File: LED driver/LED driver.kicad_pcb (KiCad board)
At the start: 2 copper layers, 49 parts, among them J1 Conn_VCC, J2 Conn_LED, J3 Conn_UART, J4 Conn_01x10, P1 USB_C_Plug_USB2.0, Q1 IRFZ44NS, Q2 IRFZ44NS, Q3 IRFZ44NS, Q4 IRFZ44NS, Q5 IRFZ44NS, SW1 SW_Push, U1 ESP32-S2-WROVER-I, U2 MP2359

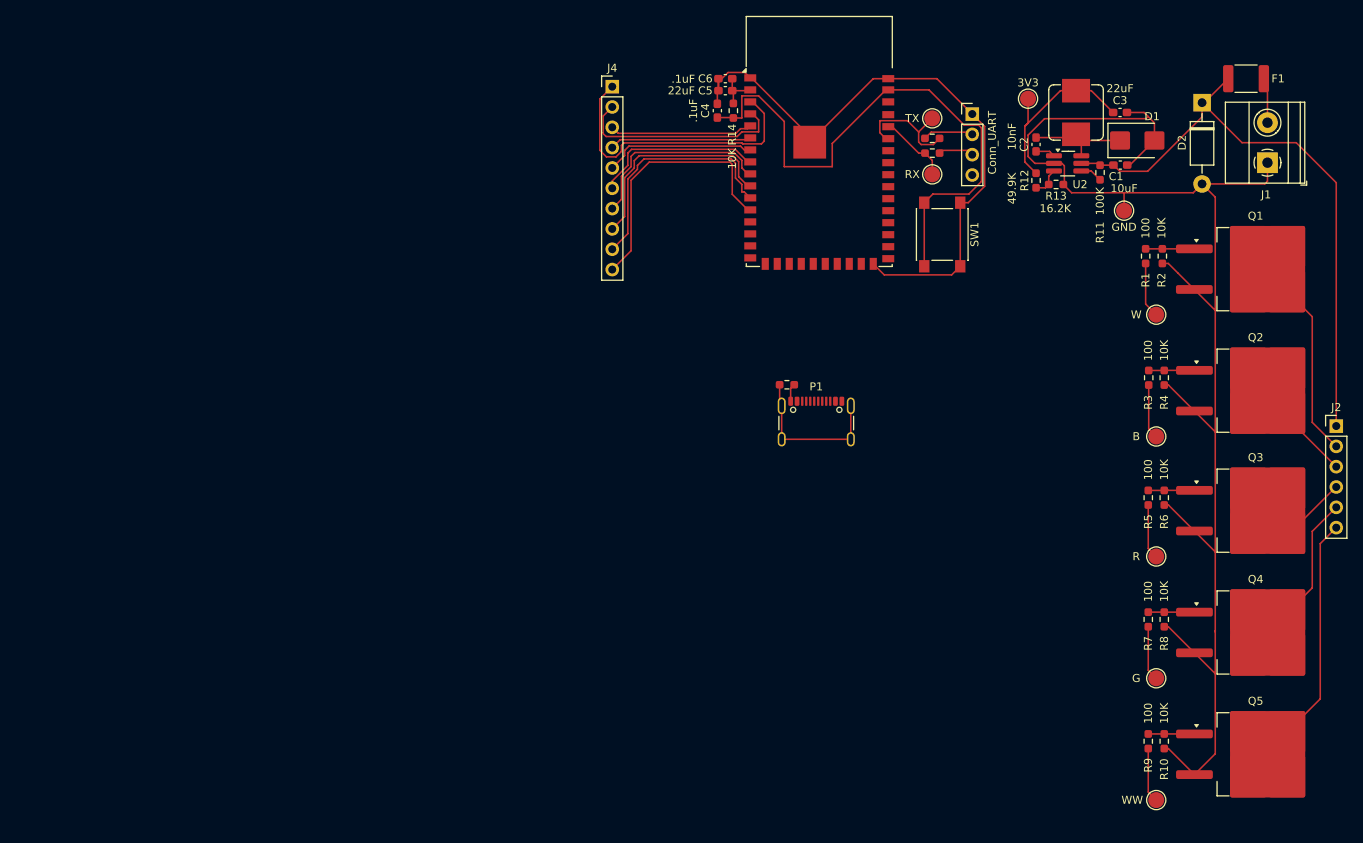
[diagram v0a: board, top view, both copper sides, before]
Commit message: update led driver, add turn signals
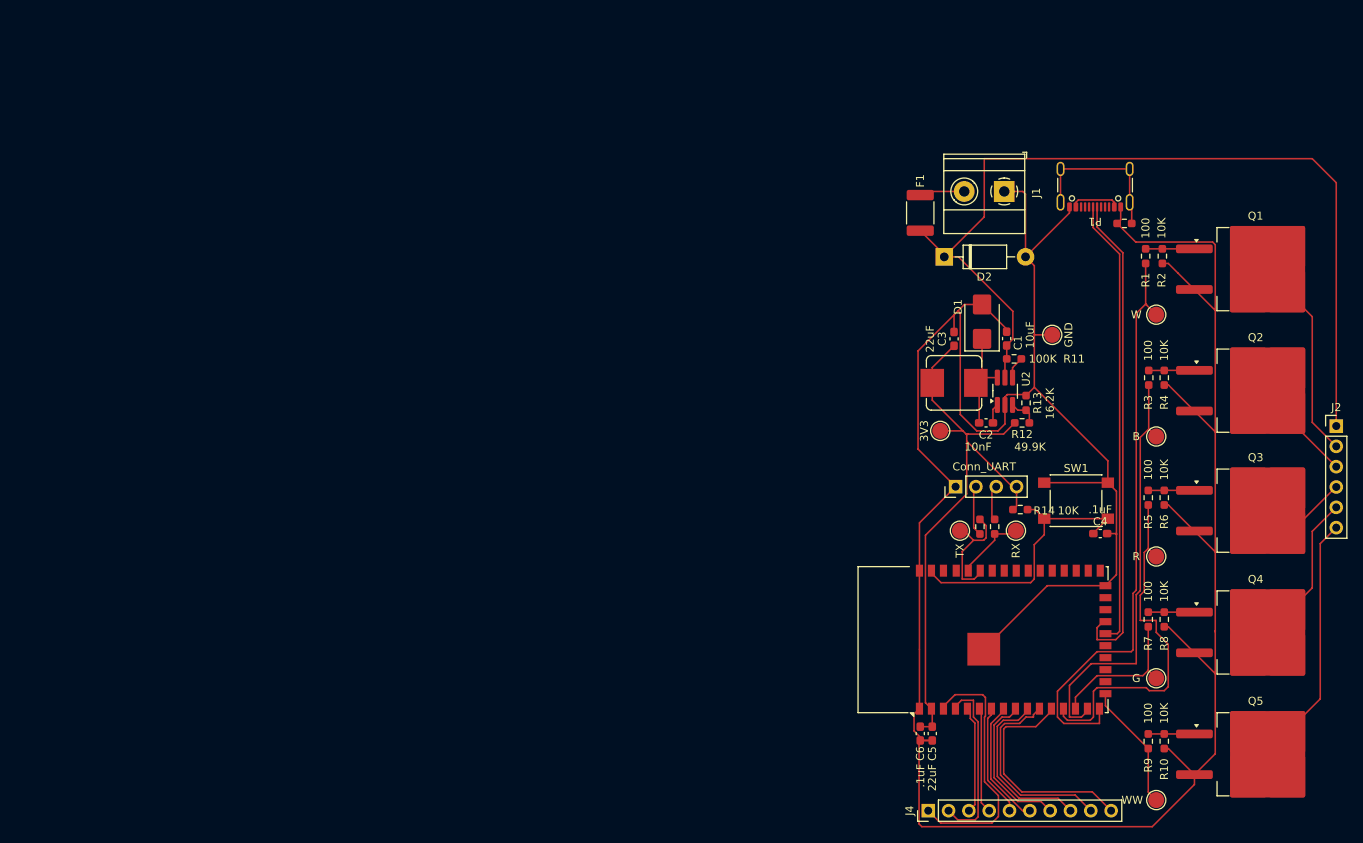
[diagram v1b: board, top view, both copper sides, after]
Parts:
- moved J4 98.7 mm to (157.5, 118.5), turned to 90 degrees
- moved C6 85.4 mm to (156.5, 108.9), turned to -90 degrees
- moved C5 84.4 mm to (158.0, 108.9), turned to -90 degrees
- moved C4 71.3 mm to (179.0, 83.9), turned to 180 degrees
- moved U1 63.3 mm to (168.2, 97.1), turned to 90 degrees
- moved R14 61.4 mm to (169.0, 80.9), turned to 0 degrees
- moved TP7 51.7 mm to (161.5, 83.5), turned to 90 degrees
- moved R15 48.9 mm to (164.0, 83.0), turned to 90 degrees
- moved R17 47.3 mm to (165.8, 83.0), turned to -90 degrees
- moved P1 47.1 mm to (178.4, 39.4), turned to 180 degrees
- moved R19 46.8 mm to (182.0, 45.1), turned to 180 degrees
- moved J3 46.6 mm to (160.9, 78.0), turned to 90 degrees
- moved TP6 45.8 mm to (168.5, 83.5), turned to 90 degrees
- moved F1 44.0 mm to (156.5, 43.8), turned to 90 degrees
- moved TP9 43.0 mm to (159.0, 71.0), turned to 90 degrees
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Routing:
- net GND: track 265.6 -> 368.4 mm
- net /PWM_W: track 6.95 -> 73.3 mm
- net Net-(P1-D+): track 0.00 -> 61.0 mm
- net Net-(P1-D-): track 0.00 -> 56.3 mm
- net +3.3V: track 29.5 -> 75.9 mm
- net /PWM_B: track 6.82 -> 53.1 mm
- net +24V: track 75.8 -> 114.4 mm
- net /PWM_R: track 6.85 -> 45.4 mm
- net Net-(U1-EN): track 73.3 -> 35.0 mm
- net /PWM_G: track 6.86 -> 18.8 mm
- net /PWM_WW: track 6.86 -> 15.9 mm
- net Net-(P1-VBUS-PadA4): track 0.00 -> 6.20 mm
- net Net-(J4-Pin_6): track 21.4 -> 16.0 mm
- net Net-(J4-Pin_7): track 24.3 -> 19.0 mm
- net Net-(J4-Pin_8): track 27.1 -> 22.0 mm
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
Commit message: update LED driver
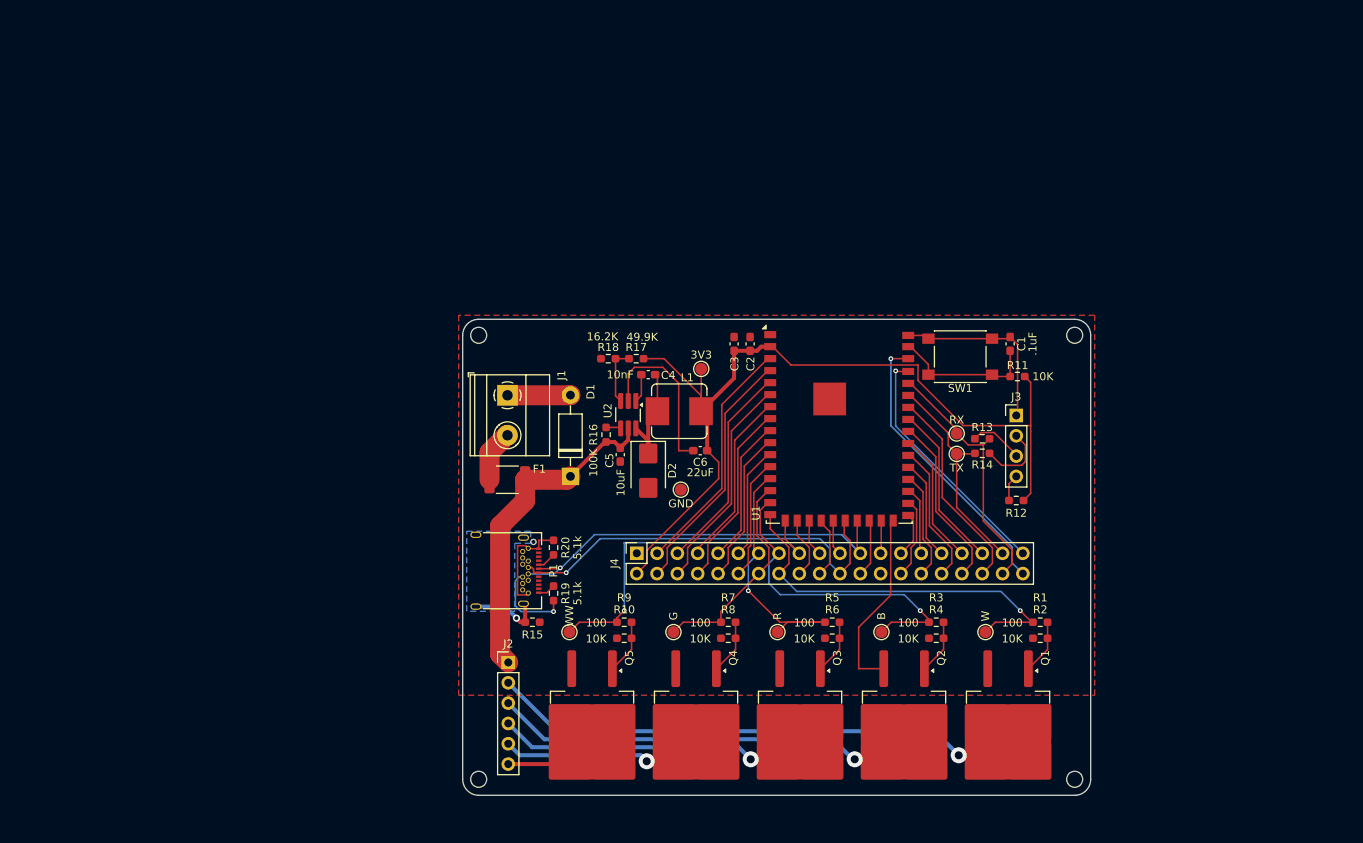
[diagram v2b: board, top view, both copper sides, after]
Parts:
- added R16: 100K, Resistor_SMD:R_0603_1608Metric_Pad0.98x0.95mm_HandSolder, F.Cu at (117.2, 71.5)
- added R18: 16.2K, Resistor_SMD:R_0603_1608Metric_Pad0.98x0.95mm_HandSolder, F.Cu at (117.5, 62.0)
- added R20: 5.1k, Resistor_SMD:R_0603_1608Metric_Pad0.98x0.95mm_HandSolder, F.Cu at (110.7, 85.6)
- C1: value 10uF -> .1uF
- C2: value 10nF -> .1uF
- C4: value .1uF -> 10nF
- C5: value 22uF -> 10uF
- C6: value .1uF -> 22uF
- D1: value B230A -> 1N4001; footprint Diode_SMD:D_SMB -> Diode_THT:D_DO-41_SOD81_P10.16mm_Horizontal
- D2: value 1N4001 -> B230A; footprint Diode_THT:D_DO-41_SOD81_P10.16mm_Horizontal -> Diode_SMD:D_SMB
- J4: value Conn_01x10 -> Conn_ESP32; footprint Connector_PinHeader_2.54mm:PinHeader_1x10_P2.54mm_Vertical -> Connector_PinSocket_2.54mm:PinSocket_2x20_P2.54mm_Vertical
- P1: value USB_C_Plug_USB2.0 -> USB_C_Receptacle_USB2.0; footprint Connector_USB:USB_C_Receptacle_GCT_USB4105-xx-A_16P_TopMnt_Horizontal -> Connector_USB:USB_C_Receptacle_Amphenol_12401548E4-2A
- R11: value 100K -> 10K
- R12: value 49.9K -> 0
- R13: value 16.2K -> 0
- R14: value 10K -> 0
- R17: value 0 -> 49.9K
- R19: value 0 -> 5.1k
- TP1, TP2, TP3, TP4, TP5: footprint TestPoint:TestPoint_Pad_D2.0mm -> TestPoint:TestPoint_Pad_D1.5mm
- TP6: value RX -> GND; footprint TestPoint:TestPoint_Pad_D2.0mm -> TestPoint:TestPoint_Pad_D1.5mm
- TP7: value TX -> 3V3; footprint TestPoint:TestPoint_Pad_D2.0mm -> TestPoint:TestPoint_Pad_D1.5mm
- TP8: value GND -> RX; footprint TestPoint:TestPoint_Pad_D2.0mm -> TestPoint:TestPoint_Pad_D1.5mm
- TP9: value 3V3 -> TX; footprint TestPoint:TestPoint_Pad_D2.0mm -> TestPoint:TestPoint_Pad_D1.5mm
- moved J2 107.6 mm to (105.0, 100.0)
- moved P1 89.3 mm to (103.8, 88.5), turned to -90 degrees
- moved R19 85.0 mm to (110.7, 91.3), turned to 90 degrees
- moved Q5 83.0 mm to (115.5, 108.4), turned to -90 degrees
- moved TP5 76.3 mm to (112.7, 96.2), turned to -90 degrees
- moved Q4 71.0 mm to (128.5, 108.4), turned to -90 degrees
- moved R10 68.7 mm to (119.5, 96.9), turned to 180 degrees
- moved R9 67.2 mm to (119.5, 94.9), turned to 180 degrees
- moved J1 67.1 mm to (104.9, 66.6), turned to -90 degrees
- moved Q1 65.4 mm to (167.5, 108.4), turned to -90 degrees
- moved Q3 63.2 mm to (141.5, 108.4), turned to -90 degrees
- moved F1 61.5 mm to (104.9, 77.1), turned to 180 degrees
- moved Q2 61.1 mm to (154.5, 108.4), turned to -90 degrees
- moved TP4 60.6 mm to (125.7, 96.2), turned to -90 degrees
- moved C4 59.9 mm to (122.5, 64.0), turned to 0 degrees
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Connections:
- C1 pad 1: +24V -> GND
- C1 pad 2: GND -> Net-(U1-EN)
- C2 pad 1: Net-(U2-BST) -> +3.3V
- C2 pad 2: Net-(D1-K) -> GND
- C4 pad 1: GND -> Net-(U2-BST)
- C4 pad 2: Net-(U1-EN) -> Net-(D2-K)
- C5 pad 1: +3.3V -> +24V
- D1 pad 1: Net-(D1-K) -> +24V
- D2 pad 1: +24V -> Net-(D2-K)
- J3 pad 4: +3.3V -> Net-(J3-Pin_4)
- J4 pad 1: Net-(J4-Pin_1) -> GND
- J4 pad 10: Net-(J4-Pin_10) -> /10
- J4 pad 2: Net-(J4-Pin_2) -> +3.3V
- J4 pad 3: Net-(J4-Pin_3) -> /3
- J4 pad 4: Net-(J4-Pin_4) -> /4
- J4 pad 5: Net-(J4-Pin_5) -> /5
- J4 pad 6: Net-(J4-Pin_6) -> /6
- J4 pad 7: Net-(J4-Pin_7) -> /7
- J4 pad 8: Net-(J4-Pin_8) -> /8
- J4 pad 9: Net-(J4-Pin_9) -> /9
- L1 pad 1: Net-(D1-K) -> Net-(D2-K)
- P1 pad A4: Net-(P1-VBUS-PadA4) -> unconnected-(P1-VBUS-PadA4)_2
- P1 pad A5: unconnected-(P1-CC-PadA5) -> Net-(P1-CC1)
- P1 pad A6: Net-(P1-D+) -> /23
- P1 pad A7: Net-(P1-D-) -> /22
- P1 pad A9: Net-(P1-VBUS-PadA4) -> unconnected-(P1-VBUS-PadA4)_0
- P1 pad B4: Net-(P1-VBUS-PadA4) -> unconnected-(P1-VBUS-PadA4)_1
- P1 pad B5: unconnected-(P1-VCONN-PadB5) -> Net-(P1-CC2)
- P1 pad B6: (no net) -> /23
- P1 pad B7: (no net) -> /22
- P1 pad B9: Net-(P1-VBUS-PadA4) -> unconnected-(P1-VBUS-PadA4)
- R1 pad 2: /PWM_W -> /16
- R11 pad 1: Net-(U2-EN) -> +3.3V
- R11 pad 2: +24V -> Net-(U1-EN)
- R12 pad 1: Net-(U2-FB) -> Net-(J3-Pin_4)
- R13 pad 1: GND -> Net-(J3-Pin_3)
- R13 pad 2: Net-(U2-FB) -> /38
- R14 pad 1: +3.3V -> Net-(J3-Pin_2)
- R14 pad 2: Net-(U1-EN) -> /37
- R15 pad 1: Net-(J3-Pin_2) -> Net-(P1-SHIELD)
- R15 pad 2: Net-(U1-TXD0) -> GND
- R17 pad 1: Net-(J3-Pin_3) -> Net-(U2-FB)
- R17 pad 2: Net-(U1-RXD0) -> +3.3V
- R19 pad 1: Net-(P1-SHIELD) -> Net-(P1-CC2)
- R3 pad 2: /PWM_B -> /15
- R5 pad 2: /PWM_R -> /13
- R7 pad 2: /PWM_G -> /14
- R9 pad 2: /PWM_WW -> /17
- TP1 pad 1: /PWM_W -> /16
- TP2 pad 1: /PWM_B -> /15
- TP3 pad 1: /PWM_R -> /13
- TP4 pad 1: /PWM_G -> /14
- TP5 pad 1: /PWM_WW -> /17
- TP6 pad 1: Net-(U1-RXD0) -> GND
- TP7 pad 1: Net-(U1-TXD0) -> +3.3V
- TP8 pad 1: GND -> /38
- TP9 pad 1: +3.3V -> /37
- U1 pad 10: Net-(J4-Pin_8) -> /10
- U1 pad 11: Net-(J4-Pin_9) -> /11
- U1 pad 12: Net-(J4-Pin_10) -> /12
- U1 pad 13: /PWM_R -> /13
- U1 pad 14: /PWM_G -> /14
- U1 pad 15: /PWM_B -> /15
- U1 pad 16: /PWM_W -> /16
- U1 pad 17: /PWM_WW -> /17
- U1 pad 18: unconnected-(U1-IO15-Pad18) -> /18
- U1 pad 19: unconnected-(U1-IO16-Pad19) -> /19
- U1 pad 20: unconnected-(U1-IO17-Pad20) -> /20
- U1 pad 21: unconnected-(U1-IO18-Pad21) -> /21
- U1 pad 22: Net-(P1-D-) -> /22
- U1 pad 23: Net-(P1-D+) -> /23
- U1 pad 24: unconnected-(U1-IO21-Pad24) -> /24
- U1 pad 25: unconnected-(U1-IO26-Pad25) -> /25
- U1 pad 27: unconnected-(U1-IO33-Pad27) -> /27
- U1 pad 28: unconnected-(U1-IO34-Pad28) -> /28
- U1 pad 29: unconnected-(U1-IO35-Pad29) -> /29
- U1 pad 3: Net-(J4-Pin_1) -> /3
- U1 pad 30: unconnected-(U1-IO36-Pad30) -> /30
- U1 pad 31: unconnected-(U1-IO37-Pad31) -> /31
- U1 pad 32: unconnected-(U1-IO38-Pad32) -> /32
- U1 pad 33: unconnected-(U1-IO39-Pad33) -> /33
- U1 pad 34: unconnected-(U1-IO40-Pad34) -> /34
- U1 pad 35: unconnected-(U1-IO41-Pad35) -> /35
- U1 pad 36: unconnected-(U1-IO42-Pad36) -> /36
- U1 pad 37: Net-(U1-TXD0) -> /37
- U1 pad 38: Net-(U1-RXD0) -> /38
- U1 pad 39: unconnected-(U1-IO45-Pad39) -> /39
- U1 pad 4: Net-(J4-Pin_2) -> /4
- U1 pad 40: unconnected-(U1-IO46-Pad40) -> /40
- U1 pad 5: Net-(J4-Pin_3) -> /5
- U1 pad 6: Net-(J4-Pin_4) -> /6
- U1 pad 7: Net-(J4-Pin_5) -> /7
- U1 pad 8: Net-(J4-Pin_6) -> /8
- U1 pad 9: Net-(J4-Pin_7) -> /9
- U2 pad 6: Net-(D1-K) -> Net-(D2-K)
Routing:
- net GND: track 368.4 -> 92.3 mm
- net /PWM_W: track 73.3 -> 0.00 mm
- net +24V: track 114.4 -> 41.7 mm
- net Net-(P1-D+): track 61.0 -> 0.00 mm
- net Net-(P1-D-): track 56.3 -> 0.00 mm
- net /PWM_B: track 53.1 -> 0.00 mm
- net /22: track 0.00 -> 51.6 mm, vias 0 -> 1
- net /23: track 0.00 -> 51.5 mm, vias 0 -> 1
- net /16: track 0.00 -> 49.6 mm, vias 0 -> 1
- net /PWM_R: track 45.4 -> 0.00 mm
- net /17: track 0.00 -> 44.0 mm, vias 0 -> 1
- net /W: track 21.9 -> 63.8 mm, vias 0 -> 1
- net /15: track 0.00 -> 41.0 mm, vias 0 -> 1
- net /B: track 9.27 -> 49.7 mm, vias 0 -> 1
- net /40: track 0.00 -> 35.9 mm, vias 0 -> 1
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- added copper zone on F.Cu, net GND
- added copper zone on B.Cu, net Net-(P1-SHIELD)
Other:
- board outline added: 78.5 x 59.5 mm

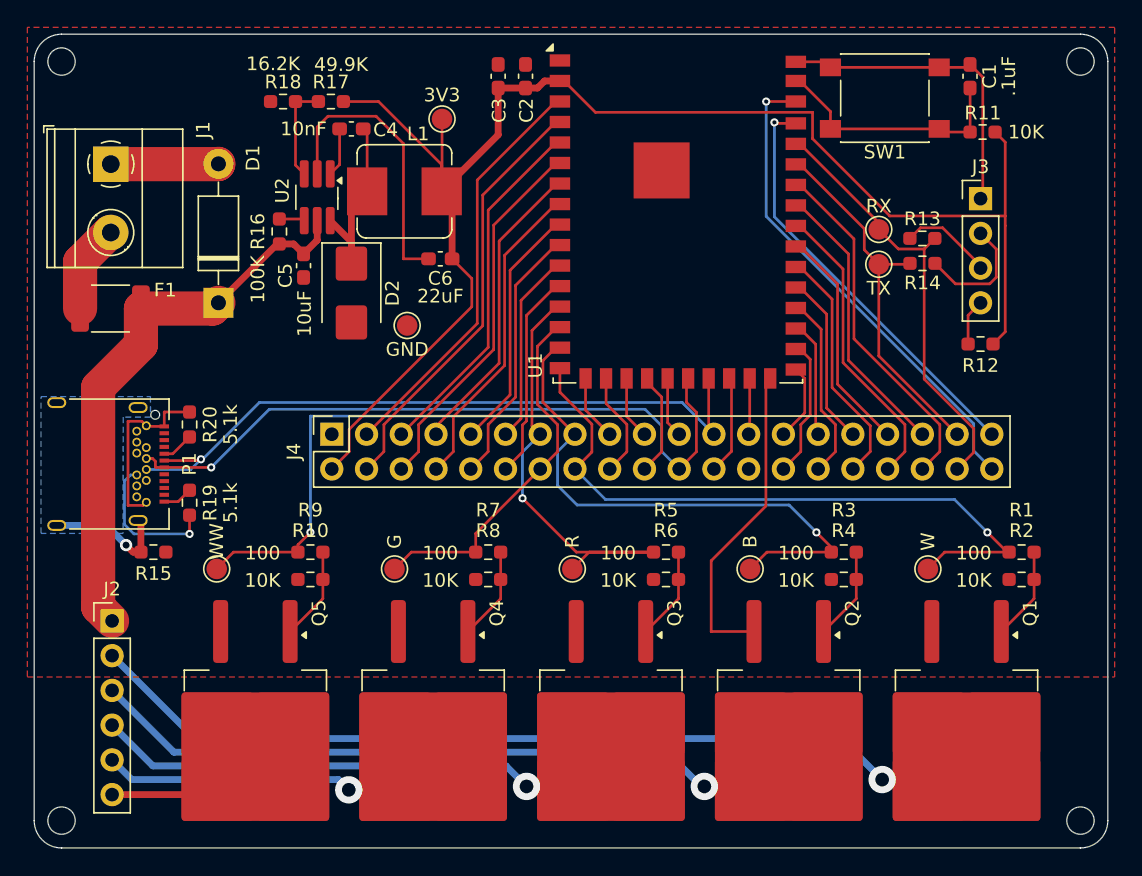
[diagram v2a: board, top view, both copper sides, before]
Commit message: update led driver
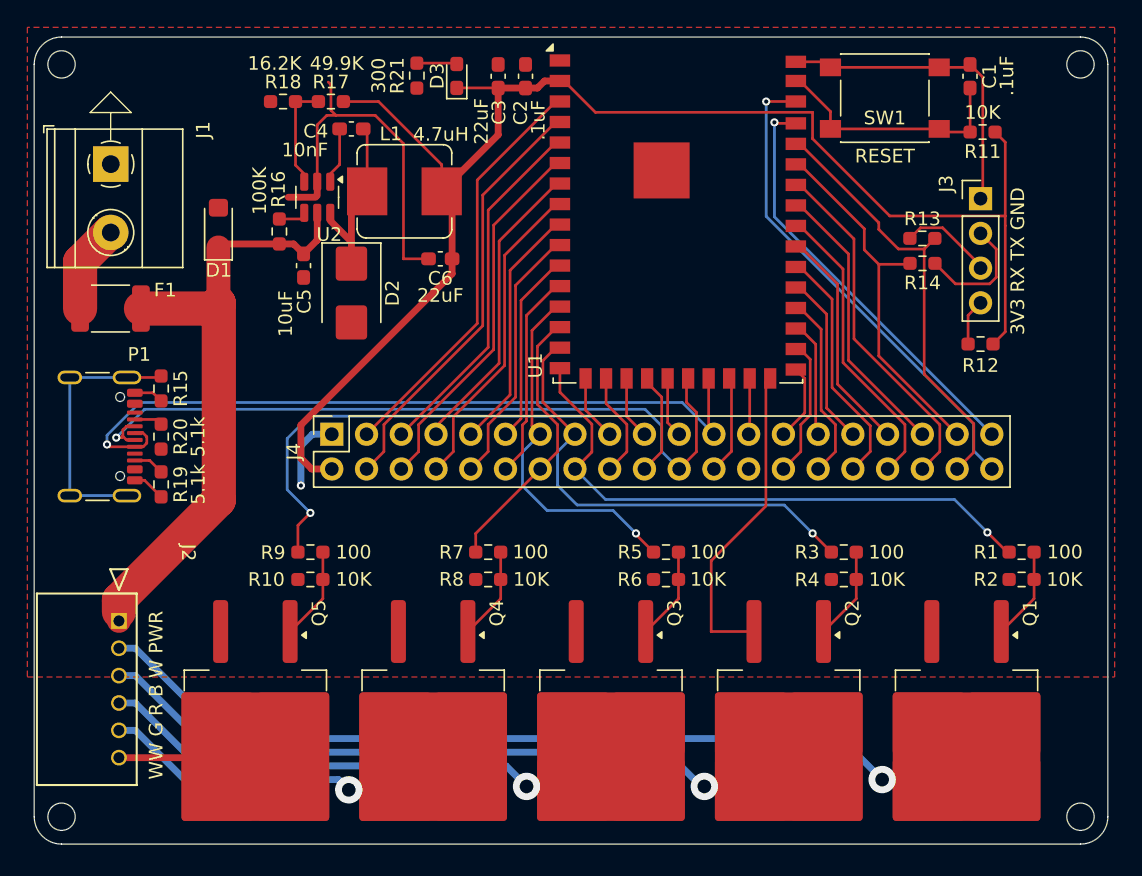
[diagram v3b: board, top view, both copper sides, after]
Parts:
- removed TP1: W, TestPoint:TestPoint_Pad_D1.5mm
- removed TP2: B, TestPoint:TestPoint_Pad_D1.5mm
- removed TP3: R, TestPoint:TestPoint_Pad_D1.5mm
- removed TP4: G, TestPoint:TestPoint_Pad_D1.5mm
- removed TP5: WW, TestPoint:TestPoint_Pad_D1.5mm
- removed TP6: GND, TestPoint:TestPoint_Pad_D1.5mm
- removed TP7: 3V3, TestPoint:TestPoint_Pad_D1.5mm
- removed TP8: RX, TestPoint:TestPoint_Pad_D1.5mm
- removed TP9: TX, TestPoint:TestPoint_Pad_D1.5mm
- added D3: PWR_LED, Diode_SMD:D_0603_1608Metric_Pad1.05x0.95mm_HandSolder, F.Cu at (130.2, 60.1)
- added R21: 300, Custom:R_0603_HandSolder_ValuePrinted, F.Cu at (127.3, 60.1)
- C1, C2, C3, C4, C5, C6: footprint Capacitor_SMD:C_0603_1608Metric_Pad1.08x0.95mm_HandSolder -> Custom:C_0603_HandSolder_ValuePrinted
- D1: value 1N4001 -> SMF24A; footprint Diode_THT:D_DO-41_SOD81_P10.16mm_Horizontal -> Diode_SMD:D_SMF
- F1: value Polyfuse -> 24V 10A
- J2: footprint Connector_PinHeader_2.54mm:PinHeader_1x06_P2.54mm_Vertical -> footprints:CON_532540670_MOL
- P1: footprint Connector_USB:USB_C_Receptacle_Amphenol_12401548E4-2A -> Connector_USB:USB_C_Receptacle_GCT_USB4105-xx-A_16P_TopMnt_Horizontal
- R1, R10, R11, R16, R17, R18, R19, R2, R20, R3, R4, R5, R6, R7, R8, R9: footprint Resistor_SMD:R_0603_1608Metric_Pad0.98x0.95mm_HandSolder -> Custom:R_0603_HandSolder_ValuePrinted
- U1: footprint RF_Module:ESP32-S2-WROVER -> Custom:ESP32-S2-WROVER
- U2: footprint Package_TO_SOT_SMD:TSOT-23-6_HandSoldering -> Package_TO_SOT_SMD:TSOT-23-6
- moved R15 12.0 mm to (108.6, 83.0), turned to -90 degrees
- moved D1 5.50 mm to (112.8, 71.2)
- moved R19 2.47 mm to (108.6, 90.0), turned to -90 degrees
- moved R20 2.26 mm to (108.6, 86.5), turned to -90 degrees
- moved P1 2.17 mm to (103.0, 86.5)
- moved J2 0.50 mm to (105.5, 100.0), turned to -90 degrees
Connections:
- net Net-(J3-Pin_2) renamed /TX
- net Net-(J3-Pin_3) renamed /RX
- J4 pad 26: /26 -> unconnected-(J4-Pin_26-Pad26)
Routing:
- net Net-(P1-SHIELD): track 9.36 -> 19.6 mm, vias 1 -> 0
- net Net-(P1-CC2): track 10.7 -> 2.27 mm, vias 1 -> 0
- net GND: track 92.3 -> 84.8 mm, vias 0 -> 1
- net /13: track 33.5 -> 26.6 mm
- net /15: track 41.0 -> 34.3 mm
- net /14: track 26.8 -> 20.4 mm
- net /16: track 49.6 -> 43.1 mm
- net /17: track 44.0 -> 39.0 mm
- net /23: track 51.5 -> 55.8 mm
- net +24V: track 41.7 -> 45.8 mm
- net /22: track 51.6 -> 55.4 mm
- net Net-(D2-K): track 14.8 -> 11.6 mm
- net Net-(D3-A): track 0.00 -> 2.94 mm
- net +3.3V: track 109.8 -> 109.0 mm
- removed copper zone on B.Cu, net Net-(P1-SHIELD)
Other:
- board size 78.5 x 59.5 mm -> 78.5 x 59 mm
- board text added: "3V3 RX TX GND"
- board text added: "RESET"
- board text added: "WW G R B W PWR"
